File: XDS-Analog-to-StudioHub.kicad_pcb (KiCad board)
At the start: 2 copper layers, 74.6 x 33.6 mm, 13 parts, among them J1 RJ45_Shielded, J2 DB9_Male

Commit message: Initial Commit
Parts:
- J2: value DB9_Male -> DB9_Female
- JP8: value Shield-Shield -> SHLD-SHLD
- JP9: value Ground to Shield -> GND-SHLD
- moved J1 36.2 mm to (123.7, 87.2)
- moved JP10 16.6 mm to (113.0, 91.6)
- moved JP11 16.6 mm to (113.0, 95.3)
- moved JP5 8.49 mm to (120.8, 102.4)
- moved JP9 8.49 mm to (120.7, 106.1)
- moved JP8 8.49 mm to (120.7, 109.8)
- moved JP3 6.37 mm to (113.0, 87.9)
- moved JP1 1.25 mm to (110.4, 98.9)
- moved JP2 1.25 mm to (110.4, 102.6)
- moved JP4 1.02 mm to (113.0, 84.2)
- moved JP7 0.12 mm to (113.0, 109.9)
- moved JP6 0.12 mm to (113.0, 106.2)
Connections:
- JP5 pad 2: Net-(J2-Pad2) -> Net-(JP5-Pad2)
- JP8 pad 2: Net-(J2-Pad0) -> (no net)
- JP9 pad 2: Net-(J2-Pad2) -> Net-(JP5-Pad2)
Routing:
- net Net-(J1-Pad6): track 1.10 -> 36.9 mm
- net Net-(J1-Pad1): track 0.00 -> 34.4 mm
- net Net-(J1-Pad3): track 1.71 -> 31.2 mm
- net Net-(J1-Pad2): track 0.00 -> 26.6 mm
- net Net-(J2-Pad9): track 0.37 -> 15.4 mm
- net Net-(J1-Pad4): track 0.00 -> 12.6 mm
- net Net-(J2-Pad5): track 0.94 -> 11.1 mm
- net Net-(J2-Pad3): track 4.49 -> 10.3 mm
- net Net-(J2-Pad8): track 17.6 -> 13.5 mm
- net Net-(JP5-Pad2): track 0.00 -> 3.66 mm
- net Net-(J2-Pad2): track 15.0 -> 11.5 mm
- added copper zone on F.Cu, net Net-(J1-PadSH)
- added copper zone on B.Cu, net Net-(J2-Pad0)
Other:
- board size 74.6 x 33.6 mm -> 39.6 x 31.6 mm
- net class Default: clearance 0.2 -> 0.05; trace_width 0.25 -> 0.2
- rule trace_clearance: 0.2 -> 0.05
- board text added: "RJ45 to XDS"
- board text added: "Steve Rubin ser@rubinbroadcasting.com"

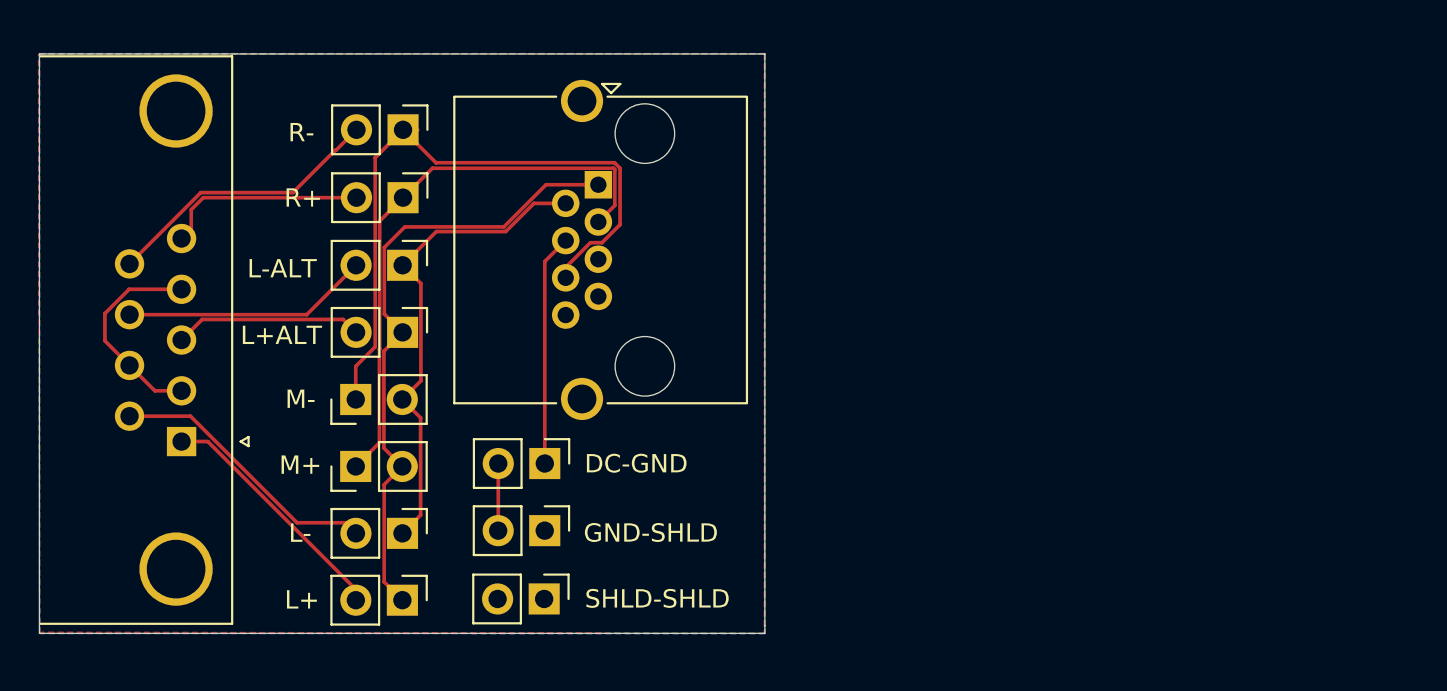
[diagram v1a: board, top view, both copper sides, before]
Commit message: corrected grounding issue
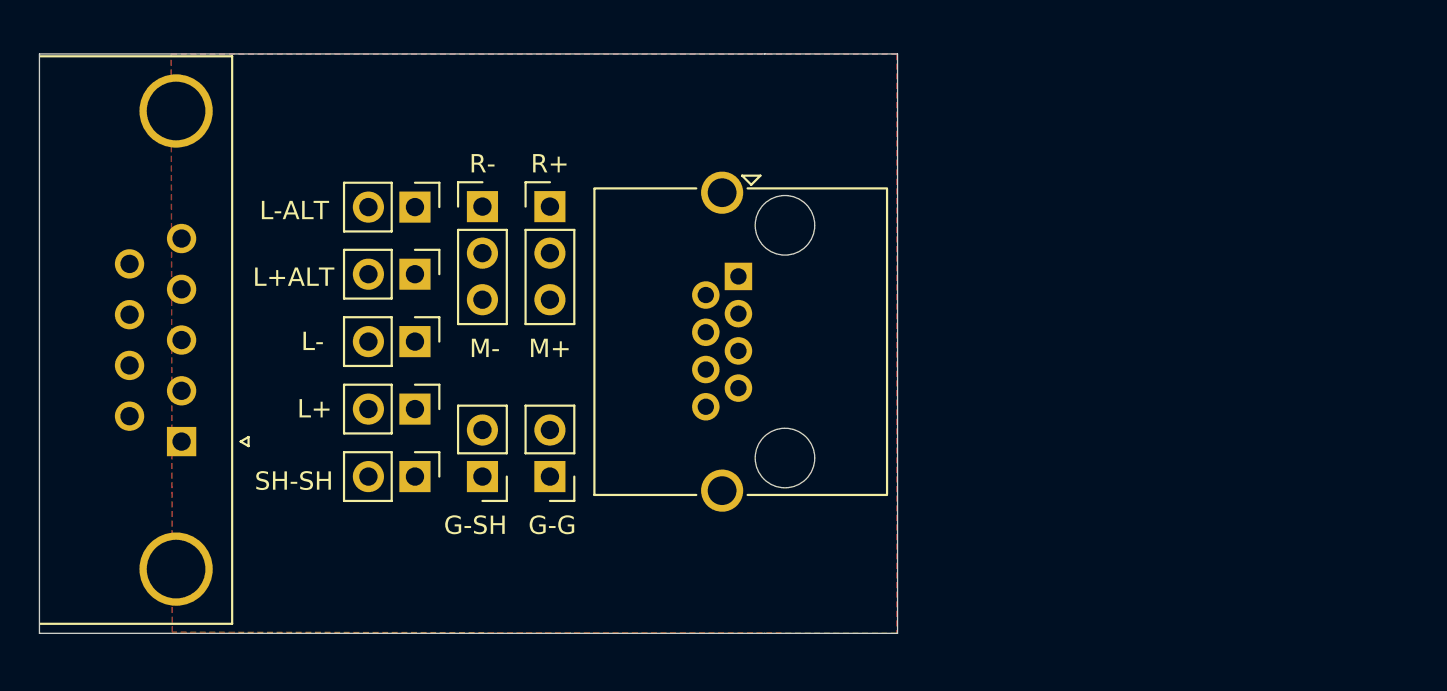
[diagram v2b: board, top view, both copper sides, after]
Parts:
- removed JP1: M-, Connector_PinHeader_2.54mm:PinHeader_1x02_P2.54mm_Vertical
- removed JP2: M+, Connector_PinHeader_2.54mm:PinHeader_1x02_P2.54mm_Vertical
- removed JP3: R+, Connector_PinHeader_2.54mm:PinHeader_1x02_P2.54mm_Vertical
- removed JP4: R-, Connector_PinHeader_2.54mm:PinHeader_1x02_P2.54mm_Vertical
- added R+: R+, Connector_PinHeader_2.54mm:PinHeader_1x03_P2.54mm_Vertical, F.Cu at (121.0, 88.4)
- added R-: R-, Connector_PinHeader_2.54mm:PinHeader_1x03_P2.54mm_Vertical, F.Cu at (117.3, 88.4)
- JP5: value DC-GND -> G-G
- JP8: value SHLD-SHLD -> SH-SH
- JP9: value GND-SHLD -> G-SH
- moved JP6 10.5 mm to (113.7, 95.8)
- moved JP7 10.5 mm to (113.7, 99.4)
- moved JP8 9.71 mm to (113.7, 103.1)
- moved J1 9.14 mm to (131.3, 92.2)
- moved JP9 4.50 mm to (117.3, 103.1), turned to 180 degrees
- moved JP10 3.25 mm to (113.7, 88.4)
- moved JP11 3.25 mm to (113.7, 92.1)
- moved JP5 0.76 mm to (121.0, 103.1), turned to 180 degrees
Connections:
- JP5 pad 2: Net-(JP5-Pad2) -> Net-(J2-Pad2)
- JP8 pad 2: (no net) -> Net-(J2-Pad0)
- JP9 pad 2: Net-(JP5-Pad2) -> Net-(J2-Pad2)
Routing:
- net Net-(J1-Pad6): track 36.9 -> 0.00 mm
- net Net-(J1-Pad1): track 34.4 -> 0.00 mm
- net Net-(J1-Pad3): track 31.2 -> 0.00 mm
- net Net-(J1-Pad2): track 26.6 -> 0.00 mm
- net Net-(J2-Pad9): track 15.4 -> 0.00 mm
- net Net-(J2-Pad6): track 15.0 -> 0.00 mm
- net Net-(J2-Pad8): track 13.5 -> 0.00 mm
- net Net-(J2-Pad1): track 13.4 -> 0.00 mm
- net Net-(J1-Pad4): track 12.6 -> 0.00 mm
- net Net-(J2-Pad2): track 11.5 -> 0.00 mm
- net Net-(J2-Pad5): track 11.1 -> 0.00 mm
- net Net-(J2-Pad3): track 10.3 -> 0.00 mm
- net Net-(JP5-Pad2): track 3.66 -> 0.00 mm
- removed copper zone on B.Cu, net Net-(J2-Pad0)
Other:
- board size 39.6 x 31.6 mm -> 46.8 x 31.6 mm
- board text added: "M+"
- board text added: "M-"

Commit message: fixed missing grounds
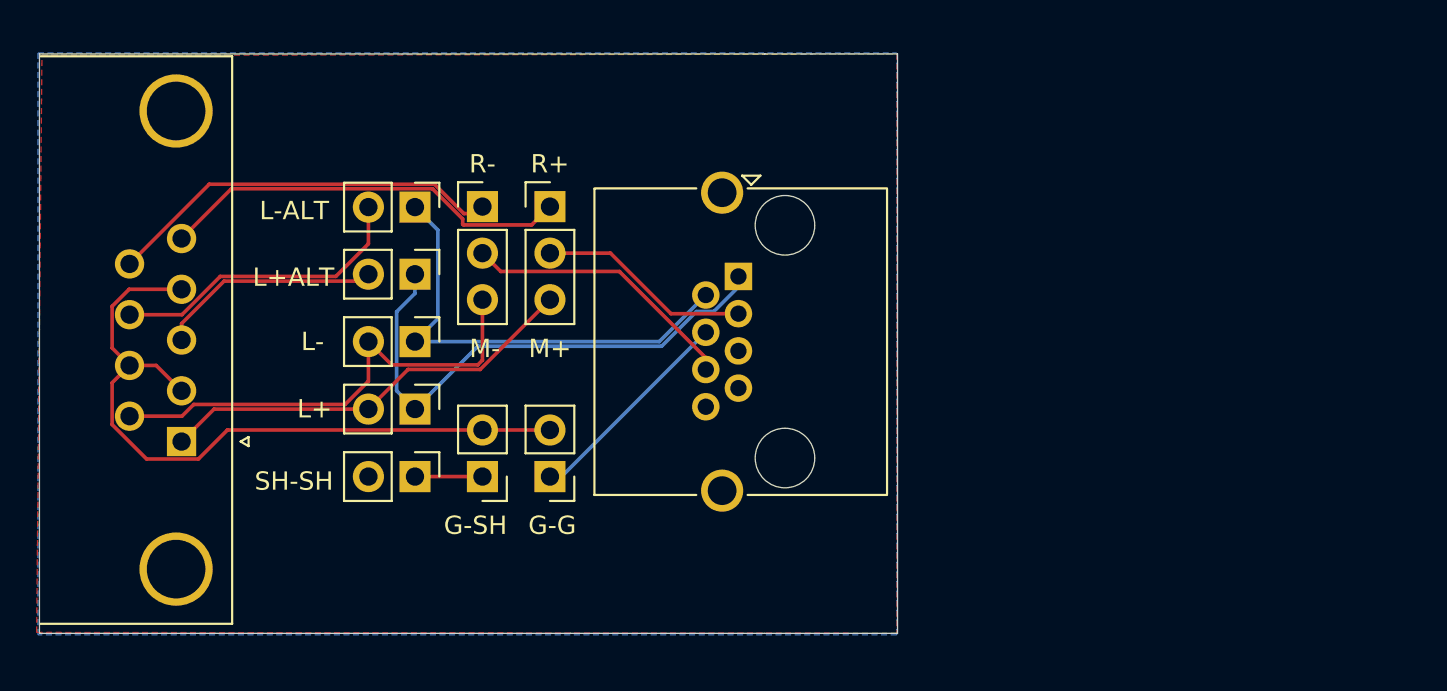
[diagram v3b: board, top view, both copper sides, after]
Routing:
- net Net-(J2-Pad2): track 0.00 -> 40.2 mm
- net Net-(J1-Pad1): track 0.00 -> 29.2 mm
- net Net-(J2-Pad6): track 0.00 -> 26.1 mm
- net Net-(J1-Pad2): track 0.00 -> 25.3 mm
- net Net-(J2-Pad1): track 0.00 -> 23.3 mm
- net Net-(J2-Pad5): track 0.00 -> 22.6 mm
- net Net-(J2-Pad9): track 0.00 -> 21.9 mm
- net Net-(J2-Pad8): track 0.00 -> 16.6 mm
- net Net-(J1-Pad6): track 0.00 -> 15.2 mm
- net Net-(J2-Pad3): track 0.00 -> 12.2 mm
- net Net-(J1-Pad4): track 0.00 -> 11.8 mm
- net Net-(J1-Pad3): track 0.00 -> 11.7 mm
- net Net-(J1-PadSH): track 0.00 -> 3.68 mm
- added copper zone on B.Cu, net Net-(J2-Pad0)
